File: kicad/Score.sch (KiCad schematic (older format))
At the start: 33 parts, among them J401 power, J402 Reset, U401 LM393, U402 TL082, U403 TL082, U404 TL082, U405 4017

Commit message: Quick fix and documentation
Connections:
- net Rampe_Point renamed Ramp_score
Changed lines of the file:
@@
 	3450 1250 4000 1250
 Text HLabel 6600 1750 0    50   Input ~ 0
-Rampe_Point
+Ramp_score
 $Comp
 L Device:R R401
@@
 Connection ~ 7400 1500
 Text HLabel 6600 3500 0    50   Input ~ 0
-Rampe_Point
+Ramp_score
 $Comp
 L Amplifier_Operational:TL082 U?
@@
 Wire Wire Line
 	3950 2750 4000 2750
+Connection ~ 4650 2650
+Wire Wire Line
+	4650 2650 4750 2650
 Wire Bus Line
 	3150 4250 3150 5550
 Wire Bus Line
 	3150 4250 4200 4250
-Connection ~ 4650 2650
-Wire Wire Line
-	4650 2650 4750 2650
 $EndSCHEMATC

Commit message: tests and doc ok
still need some scoring options
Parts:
- removed unit 1 of U402
- removed unit 2 of U402
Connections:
- net Pos_X: now also U401.2 (-), U401.5 (+); no longer U401.3 (+), U401.6 (_)
- net at R405.1, R409.1: now also U401.3 (+); no longer U401.2 (-)
- net at R406.1, R410.1: now also U401.6 (_); no longer U401.5 (+)
- net sheet5C9A25F6/Edge renamed Left counter/Edge
- net sheet5C9A25F6/Score_Display renamed Left counter/Score_Display
- net sheet5CC39077/Edge renamed Right counter/Edge
- net sheet5CC39077/Score_Display renamed Right counter/Score_Display
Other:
- note added: "Offset to place the score\non top of the screen"
- note added: "Open-collector:\nWhen not the current score,\ndraw a dot instead of a line"
- note added: "Reflect the current\ndisplayed line"
- note added: "The ball is at the left edge"
- note added: "The ball is at the right edge"
- note added: "VISUAL - OK"
- note added: "With carefully chosen resistors, \nwe can evenly space the \nscore lines along the X axis"

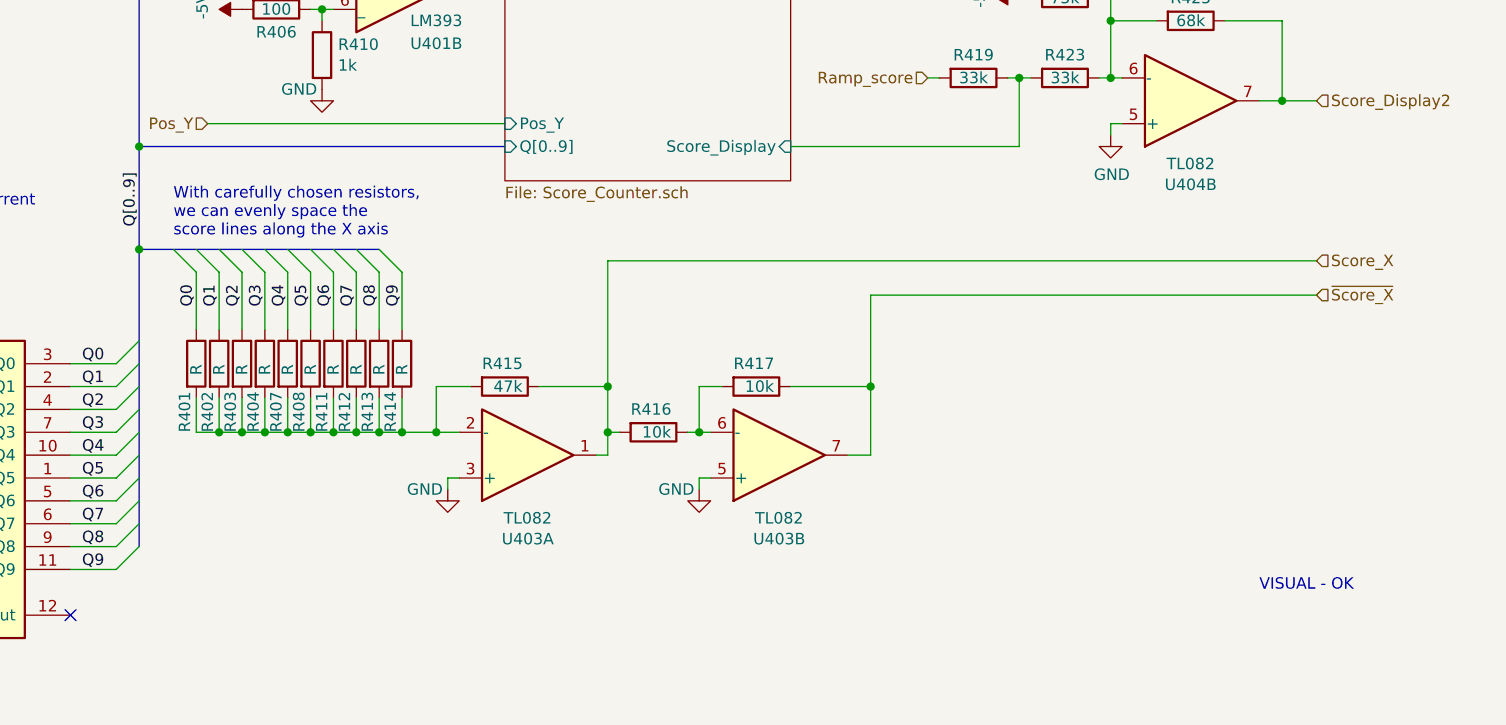
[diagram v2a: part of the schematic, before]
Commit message: Calculated DAC's resistors
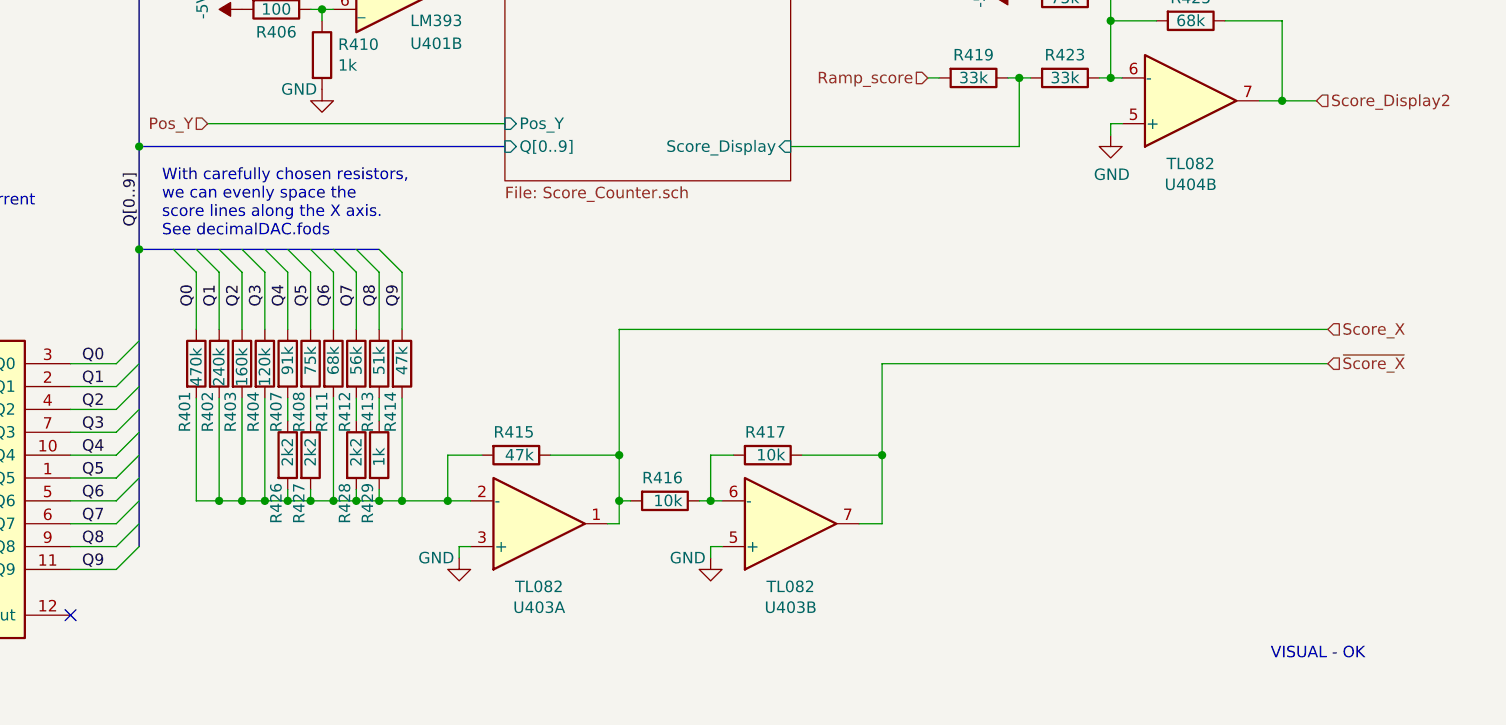
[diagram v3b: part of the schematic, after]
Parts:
- added R426, R427, R428: 2k2, Resistor_THT:R_Axial_DIN0204_L3.6mm_D1.6mm_P7.62mm_Horizontal, symbol Device:R
- added R429: 1k, Resistor_THT:R_Axial_DIN0204_L3.6mm_D1.6mm_P7.62mm_Horizontal, symbol Device:R
- R401: value R -> 470k
- R402: value R -> 240k
- R403: value R -> 160k
- R404: value R -> 120k
- R407: value R -> 91k
- R408: value R -> 75k
- R411: value R -> 68k
- R412: value R -> 56k
- R413: value R -> 51k
- R414: value R -> 47k
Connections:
- net at R401.2, R402.2, R403.2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: now also R426.2, R427.2, R428.2, R429.2; no longer R407.2, R408.2, R412.2, R413.2
- new net: R407.2, R426.1
- new net: R408.2, R427.1
- new net: R412.2, R428.1
- new net: R413.2, R429.1
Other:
- note added: "With carefully chosen resistors, \nwe can evenly space the \nscore lines along the X axis.\nSee decimalDAC.fods"
- note removed: "With carefully chosen resistors, \nwe can evenly space the \nscore lines along the X axis"
- moved on the sheet: R415, R416, R417, U403A, U403B

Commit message: Small fixes and more documentation
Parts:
- R407: value 91k -> 82k
- R426: value 2k2 -> 12k
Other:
- note added: "REALITY - OK"
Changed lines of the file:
@@
 P 3800 4750
 F 0 "R407" V 3750 4450 50  0000 L CNN
-F 1 "91k" V 3800 4700 50  0000 L CNN
+F 1 "82k" V 3800 4700 50  0000 L CNN
 F 2 "Resistor_THT:R_Axial_DIN0204_L3.6mm_D1.6mm_P7.62mm_Horizontal" V 3730 4750 50  0001 C CNN
 F 3 "~" H 3800 4750 50  0001 C CNN
@@
 Text Notes 7050 1250 0    50   ~ 0
 Offset to place the score\non top of the screen
-Text Notes 8100 6050 0    50   ~ 0
-VISUAL - OK
+Text Notes 6200 6150 0    50   ~ 0
+REALITY - OK
 $Comp
 L Device:R R426
@@
 P 3800 5150
 F 0 "R426" V 3750 4850 50  0000 L CNN
-F 1 "2k2" V 3800 5100 50  0000 L CNN
+F 1 "12k" V 3800 5050 50  0000 L CNN
 F 2 "Resistor_THT:R_Axial_DIN0204_L3.6mm_D1.6mm_P7.62mm_Horizontal" V 3730 5150 50  0001 C CNN
 F 3 "~" H 3800 5150 50  0001 C CNN
@@
 Wire Bus Line
 	3150 4250 4200 4250
+Text Notes 8150 4250 0    50   ~ 0
+VISUAL - OK
 $EndSCHEMATC
